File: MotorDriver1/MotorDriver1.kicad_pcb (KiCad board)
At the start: 2 copper layers, 60.5 x 66.5 mm, 74 parts, among them IC1 STM32C092RCT6, IC2 mcp6004-e_p, J1 GT-USB-7010ASV, J2 Conn_01x02, J3 Conn_01x02, Q1 IRLZ44N, Q2 IRLZ44N, Q3 IRLZ44N, Q4 IRLZ44N, SW1 K2-6639SP-C4SC-04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

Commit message: modifications to PCB layout
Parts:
- moved C_D1 20.5 mm to (166.2, 57.5)
- moved R17 20.5 mm to (166.3, 54.0)
- moved R18 20.5 mm to (169.8, 54.0)
- moved R19 20.5 mm to (169.8, 57.0)
- moved VR1 20.5 mm to (175.3, 54.0)
- moved VR2 20.5 mm to (183.3, 54.0)
- moved U3 9.51 mm to (175.5, 38.5), turned to 90 degrees
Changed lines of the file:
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@@
 	(footprint "Resistor_SMD:R_0402_1005Metric"
 		(layer "F.Cu")
-		(at 169 33.5)
+		(at 169.85 54)
 		(descr "Resistor SMD 0402 (1005 Metric), square (rectangular) end terminal, IPC-7351 nominal, (Body size source: IPC-SM-782 page 72, https://www.pcb-3d.com/wordpress/wp-content/uploads/ipc-sm-782a_amendment_1_and_2.pdf), generated with kicad-footprint-generator")
 		(tags "resistor")
@@
 	(footprint "Resistor_SMD:R_0402_1005Metric"
 		(layer "F.Cu")
-		(at 169 36.5)
+		(at 169.85 57)
 		(descr "Resistor SMD 0402 (1005 Metric), square (rectangular) end terminal, IPC-7351 nominal, (Body size source: IPC-SM-782 page 72, https://www.pcb-3d.com/wordpress/wp-content/uploads/ipc-sm-782a_amendment_1_and_2.pdf), generated with kicad-footprint-generator")
 		(tags "resistor")
@@
 	(footprint "Resistor_SMD:R_0402_1005Metric"
 		(layer "F.Cu")
-		(at 165.49 33.5)
+		(at 166.34 54)
 		(descr "Resistor SMD 0402 (1005 Metric), square (rectangular) end terminal, IPC-7351 nominal, (Body size source: IPC-SM-782 page 72, https://www.pcb-3d.com/wordpress/wp-content/uploads/ipc-sm-782a_amendment_1_and_2.pdf), generated with kicad-footprint-generator")
 		(tags "resistor")
@@
 	(footprint "footprintLib:XIAO-ESP32-C5-DIP"
 		(layer "F.Cu")
-		(at 175 48)
+		(at 175.5 38.5 90)
 		(property "Reference" "U3"
-			(at -0.275 -10.275 0)
+			(at -53.275 -5.775 90)
 			(unlocked yes)
 			(layer "F.SilkS")
@@
 		)
 		(property "Value" "XIAO-ESP32-C5-DIP"
-			(at 0 0 0)
+			(at 0 0 90)
 			(unlocked yes)
 			(layer "F.Fab")
@@
 		)
 		(property "Datasheet" ""
-			(at 0 0 0)
+			(at 0 0 90)
 			(unlocked yes)
 			(layer "F.Fab")
@@
 		)
 		(property "Description" ""
-			(at 0 0 0)
+			(at 0 0 90)
 			(unlocked yes)
 			(layer "F.Fab")
@@
 		(attr smd)
 		(fp_line
+			(start -8.509 -8.89)
+			(end 8.636 -8.89)
+			(stroke
+				(width 0.127)
+				(type solid)
+			)
+			(layer "F.SilkS")
+		)
+		(fp_line
 			(start -10.414 -6.985)
 			(end -10.414 6.985)
@@
 		)
 		(fp_line
-			(start -8.509 -8.89)
-			(end 8.636 -8.89)
+			(start 10.541 -4.495)
+			(end 11.551272 -4.491272)
 			(stroke
 				(width 0.127)
@@
 		)
 		(fp_line
-			(start -8.509 8.89)
-			(end 8.636 8.89)
+			(start 12.051 -3.991272)
+			(end 12.051 4.004)
 			(stroke
 				(width 0.127)
@@
 		)
 		(fp_line
-			(start 10.541 -4.495)
-			(end 11.551272 -4.491272)
+			(start 11.551 4.504)
+			(end 10.541 4.504)
 			(stroke
 				(width 0.127)
@@
 		)
 		(fp_line
-			(start 11.551 4.504)
-			(end 10.541 4.504)
+			(start -8.509 8.89)
+			(end 8.636 8.89)
 			(stroke
 				(width 0.127)
@@
 			(layer "F.SilkS")
 		)
-		(fp_line
-			(start 12.051 -3.991272)
-			(end 12.051 4.004)
+		(fp_arc
+			(start 8.636 -8.89)
+			(mid 9.983038 -8.332038)
+			(end 10.541 -6.985)
 			(stroke
 				(width 0.127)
@@
 		)
 		(fp_arc
-			(start -8.509 8.89)
-			(mid -9.856038 8.332038)
-			(end -10.414 6.985)
+			(start 11.551272 -4.491272)
+			(mid 11.904644 -4.344724)
+			(end 12.051 -3.991272)
 			(stroke
 				(width 0.127)
-				(type solid)
+				(type default)
 			)
 			(layer "F.SilkS")
 		)
 		(fp_arc
-			(start 8.636 -8.89)
-			(mid 9.983038 -8.332038)
-			(end 10.541 -6.985)
+			(start 12.051 4.004)
+			(mid 11.904553 4.357553)
+			(end 11.551 4.504)
 			(stroke
 				(width 0.127)
-				(type solid)
+				(type default)
 			)
 			(layer "F.SilkS")
@@
 		)
 		(fp_arc
-			(start 11.551272 -4.491272)
-			(mid 11.904644 -4.344724)
-			(end 12.051 -3.991272)
-			(stroke
-				(width 0.127)
-				(type default)
-			)
-			(layer "F.SilkS")
-		)
-		(fp_arc
-			(start 12.051 4.004)
-			(mid 11.904553 4.357553)
-			(end 11.551 4.504)
+			(start -8.509 8.89)
+			(mid -9.856038 8.332038)
+			(end -10.414 6.985)
 			(stroke
 				(width 0.127)
-				(type default)
+				(type solid)
 			)
 			(layer "F.SilkS")
 		)
 		(fp_circle
-			(center 9.37 -7.857)
-			(end 9.624 -7.857)
+			(center 10.25 -9)
+			(end 10.504 -9)
 			(stroke
 				(width 0.5)
@@
 		)
 		(fp_circle
-			(center 10.25 -9)
-			(end 10.504 -9)
+			(center 9.37 -7.857)
+			(end 9.624 -7.857)
 			(stroke
 				(width 0.5)
@@
 		)
 		(pad "1" smd roundrect
-			(at 7.62 -8.455 90)
+			(at 7.62 -8.455 180)
 			(size 2.432 1.524)
 			(layers "F.Cu" "F.Mask")
@@
 		)
 		(pad "1" thru_hole circle
-			(at 7.62 -7.62 90)
+			(at 7.62 -7.62 180)
 			(size 1.524 1.524)
 			(drill 0.889)
@@
 		)
 		(pad "2" smd roundrect
-			(at 5.08 -8.455 90)
+			(at 5.08 -8.455 180)
 			(size 2.432 1.524)
 			(layers "F.Cu" "F.Mask")
@@
 		)
 		(pad "2" thru_hole circle
-			(at 5.08 -7.62 90)
+			(at 5.08 -7.62 180)
 			(size 1.524 1.524)
 			(drill 0.889)
@@
 		)
 		(pad "3" smd roundrect
-			(at 2.54 -8.455 90)
+			(at 2.54 -8.455 180)
 			(size 2.432 1.524)
 			(layers "F.Cu" "F.Mask")
@@
 		)
 		(pad "3" thru_hole circle
-			(at 2.54 -7.62 90)
+			(at 2.54 -7.62 180)
 			(size 1.524 1.524)
 			(drill 0.889)
@@
 		)
 		(pad "4" smd roundrect
-			(at 0 -8.455 90)
+			(at 0 -8.455 180)
 			(size 2.432 1.524)
 			(layers "F.Cu" "F.Mask")
@@
 		)
 		(pad "4" thru_hole circle
-			(at 0 -7.62 90)
+			(at 0 -7.62 180)
 			(size 1.524 1.524)
 			(drill 0.889)
@@
 		)
 		(pad "5" smd roundrect
-			(at -2.54 -8.455 90)
+			(at -2.54 -8.455 180)
 			(size 2.432 1.524)
 			(layers "F.Cu" "F.Mask")
@@
 		)
 		(pad "5" thru_hole circle
-			(at -2.54 -7.62 90)
+			(at -2.54 -7.62 180)
 			(size 1.524 1.524)
 			(drill 0.889)
@@
 		)
 		(pad "6" smd roundrect
-			(at -5.08 -8.455 90)
+			(at -5.08 -8.455 180)
 			(size 2.432 1.524)
 			(layers "F.Cu" "F.Mask")
@@
 		)
 		(pad "6" thru_hole circle
-			(at -5.08 -7.62 90)
+			(at -5.08 -7.62 180)
 			(size 1.524 1.524)
 			(drill 0.889)
@@
 		)
 		(pad "7" smd roundrect
-			(at -7.62 -8.455 90)
+			(at -7.62 -8.455 180)
 			(size 2.432 1.524)
 			(layers "F.Cu" "F.Mask")
@@
 		)
 		(pad "7" thru_hole circle
-			(at -7.62 -7.62 90)
+			(at -7.62 -7.62 180)
 			(size 1.524 1.524)
 			(drill 0.889)
@@
 		)
 		(pad "8" thru_hole circle
-			(at -7.62 7.62 270)
+			(at -7.62 7.62)
 			(size 1.524 1.524)
 			(drill 0.889)
@@
 		)
 		(pad "8" smd roundrect
-			(at -7.62 8.455 270)
+			(at -7.62 8.455)
 			(size 2.432 1.524)
 			(layers "F.Cu" "F.Mask")
@@
 		)
 		(pad "9" thru_hole circle
-			(at -5.08 7.62 270)
+			(at -5.08 7.62)
 			(size 1.524 1.524)
 			(drill 0.889)
@@
 		)
 		(pad "9" smd roundrect
-			(at -5.08 8.455 270)
+			(at -5.08 8.455)
 			(size 2.432 1.524)
 			(layers "F.Cu" "F.Mask")
@@
 		)
 		(pad "10" thru_hole circle
-			(at -2.54 7.62 270)
+			(at -2.54 7.62)
 			(size 1.524 1.524)
 			(drill 0.889)
@@
 		)
 		(pad "10" smd roundrect
-			(at -2.54 8.455 270)
+			(at -2.54 8.455)
 			(size 2.432 1.524)
 			(layers "F.Cu" "F.Mask")
@@
 		)
 		(pad "11" thru_hole circle
-			(at 0 7.62 270)
+			(at 0 7.62)
 			(size 1.524 1.524)
 			(drill 0.889)
@@
 		)
 		(pad "11" smd roundrect
-			(at 0 8.455 270)
+			(at 0 8.455)
 			(size 2.432 1.524)
 			(layers "F.Cu" "F.Mask")
@@
 		)
 		(pad "12" thru_hole circle
-			(at 2.54 7.62 270)
+			(at 2.54 7.62)
 			(size 1.524 1.524)
 			(drill 0.889)
@@
 		)
 		(pad "12" smd roundrect
-			(at 2.54 8.455 270)
+			(at 2.54 8.455)
 			(size 2.432 1.524)
 			(layers "F.Cu" "F.Mask")
@@
 		)
 		(pad "13" thru_hole circle
-			(at 5.08 7.62 270)
+			(at 5.08 7.62)
 			(size 1.524 1.524)
 			(drill 0.889)
@@
 		)
 		(pad "13" smd roundrect
-			(at 5.08 8.455 270)
+			(at 5.08 8.455)
 			(size 2.432 1.524)
 			(layers "F.Cu" "F.Mask")
@@
 		)
 		(pad "14" thru_hole circle
-			(at 7.62 7.62 270)
+			(at 7.62 7.62)
 			(size 1.524 1.524)
 			(drill 0.889)
@@
 		)
 		(pad "14" smd roundrect
-			(at 7.62 8.455 270)
+			(at 7.62 8.455)
 			(size 2.432 1.524)
 			(layers "F.Cu" "F.Mask")
@@
 	(footprint "footprintLib:TS53YJ105MR10"
 		(layer "F.Cu")
-		(at 182.5 33.5)
+		(at 183.35 54)
 		(descr "TS53YJ105MR10-1")
 		(tags "Variable Resistor")
@@
 	(footprint "footprintLib:TS53YJ105MR10"
 		(layer "F.Cu")
-		(at 174.5 33.5)
+		(at 175.35 54)
 		(descr "TS53YJ105MR10-1")
 		(tags "Variable Resistor")
@@
 	(footprint "Capacitor_SMD:C_0201_0603Metric"
 		(layer "F.Cu")
-		(at 165.32 37)
+		(at 166.17 57.5)
 		(descr "Capacitor SMD 0201 (0603 Metric), square (rectangular) end terminal, IPC-7351 nominal, (Body size source: https://www.vishay.com/docs/20052/crcw0201e3.pdf), generated with kicad-footprint-generator")
 		(tags "capacitor")

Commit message: Re-layed out eo stuff
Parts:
- C12, C13, C14, R13, R14, U1: moved to B.Cu
- moved VR1 46.6 mm to (129.2, 60.8)
- moved VR2 46.6 mm to (137.2, 60.8)
- moved R17 29.8 mm to (137.1, 48.5)
- moved C_D1 29.8 mm to (136.9, 52.0)
- moved R18 29.8 mm to (140.6, 48.5)
- moved R19 29.8 mm to (140.6, 51.5)
- moved R15 15.3 mm to (160.0, 86.5), turned to 180 degrees
- moved R23 14.5 mm to (175.0, 51.8)
- moved R21 12.9 mm to (174.8, 53.8), turned to -90 degrees
- moved C13 11.7 mm to (168.5, 88.0)
- moved R22 11.6 mm to (173.7, 61.6), turned to 90 degrees
- moved R20 10.5 mm to (173.5, 63.6), turned to 180 degrees
- moved R12 9.70 mm to (159.5, 82.5), turned to -90 degrees
- moved C14 9.22 mm to (167.5, 90.0)
- moved U5 8.70 mm to (169.8, 53.8)
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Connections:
- IC1 pad 1: unconnected-(IC1-PC11-Pad1) -> USER_BTN
- IC1 pad 3: USER_BTN -> unconnected-(IC1-PC13-Pad3)
- U4 pad 4: FDCAN_STM -> FDCAN_RX_STM

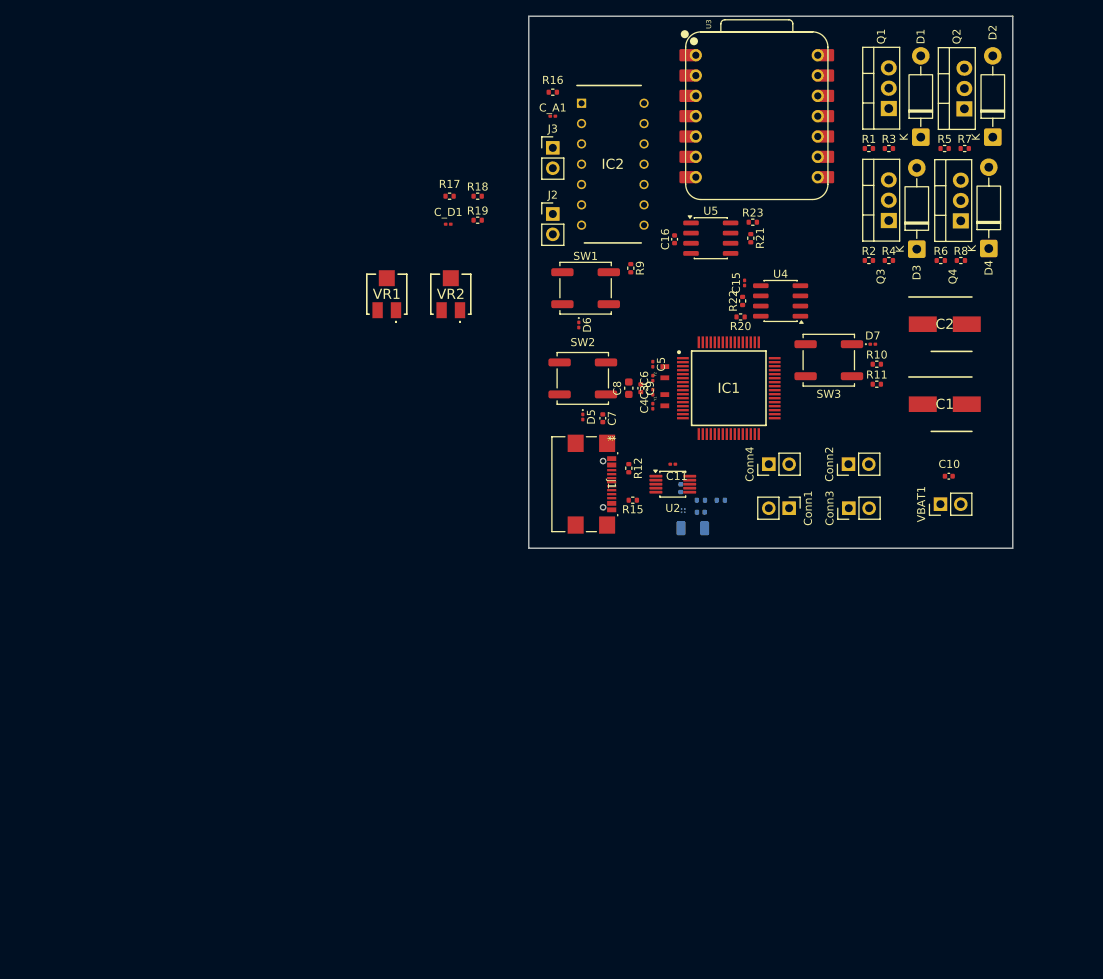
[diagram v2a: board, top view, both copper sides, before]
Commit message: component placing and first traces
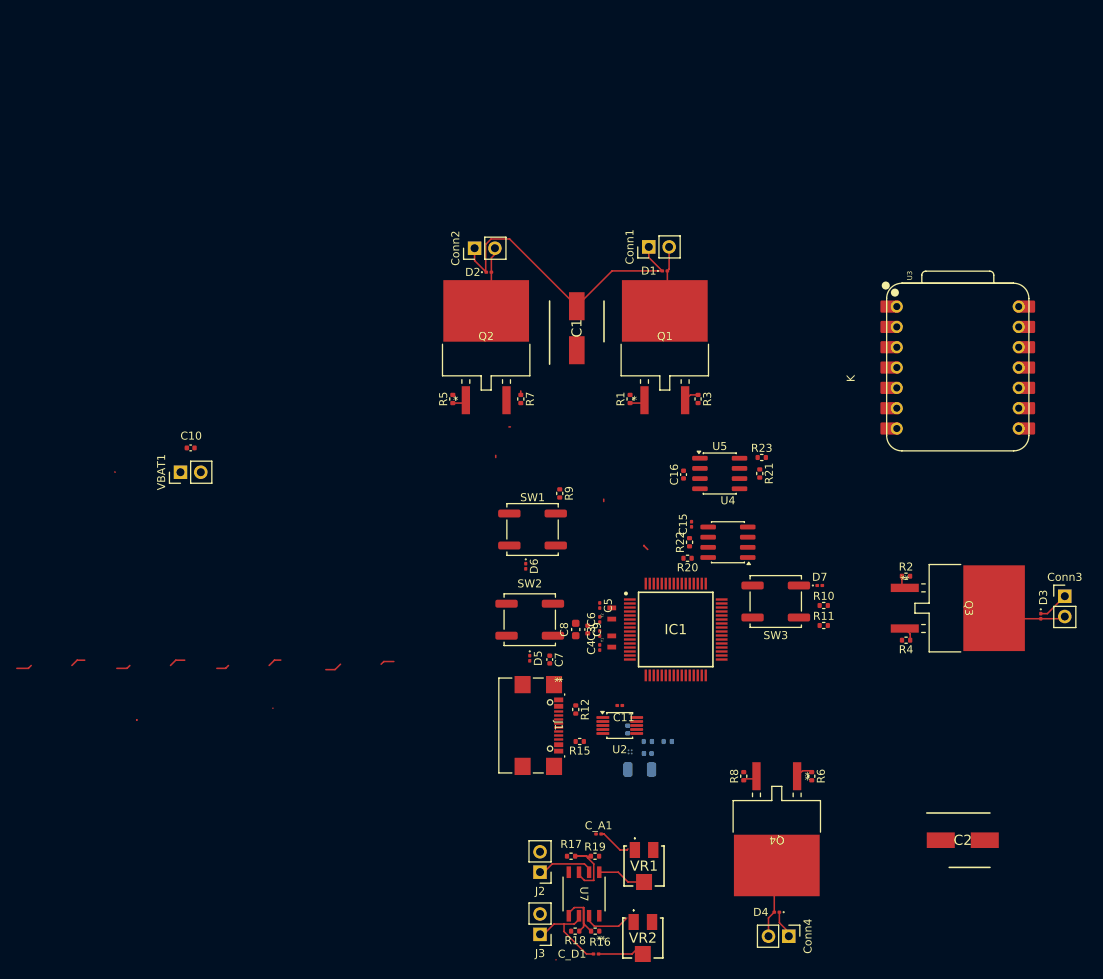
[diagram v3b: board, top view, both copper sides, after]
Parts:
- removed IC2: mcp6004-e_p, footprintLib:DIP781W56P254L1918H533Q14N
- added U7: LMV358AIDR, footprintLib:D8_TEX, F.Cu at (153.9, 135.7)
- D1, D2, D3, D4: value 1N4001 -> Power_D; footprint Diode_THT:D_DO-41_SOD81_P10.16mm_Horizontal -> Diode_SMD:D_0201_0603Metric
- Q1, Q2, Q3, Q4: value IRLZ44N -> IRLZ44NSTRLPBF; footprint Package_TO_SOT_THT:TO-220-3_Vertical -> footprintLib:NMOSGDS_D2PAK_INF
- moved R16 105.0 mm to (155.3, 140.4), turned to 180 degrees
- moved J3 98.3 mm to (148.4, 140.8), turned to 180 degrees
- moved VBAT1 95.1 mm to (103.5, 83.0)
- moved C10 94.8 mm to (104.7, 80.0)
- moved C_D1 93.1 mm to (155.4, 143.2)
- moved R18 92.7 mm to (152.8, 140.4), turned to 180 degrees
- moved C_A1 89.9 mm to (155.7, 128.2)
- moved D4 87.1 mm to (178.0, 138.0), turned to 180 degrees
- moved VR2 84.0 mm to (161.3, 141.2), turned to 180 degrees
- moved R17 83.9 mm to (152.3, 131.0)
- moved J2 82.3 mm to (148.4, 133.0), turned to 180 degrees
- moved R19 80.8 mm to (155.3, 131.0)
- moved Q4 80.8 mm to (178.0, 129.0), turned to 180 degrees
- moved VR1 78.4 mm to (161.4, 132.2), turned to 180 degrees
- moved R8 69.9 mm to (173.9, 121.0), turned to 90 degrees
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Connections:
- IC1 pad 47: Motor1_PWM -> Motor3_PWM
- IC1 pad 58: Motor3_PWM -> Motor1_PWM
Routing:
- net 5V: track 0.00 -> 46.1 mm
- net SensorDIn: track 0.00 -> 11.4 mm
- net /motorDriver/Motor4-: track 0.00 -> 10.3 mm
- net /motorDriver/Motor3-: track 0.00 -> 9.77 mm
- net SensorA_0.5V: track 0.00 -> 9.71 mm
- net /motorDriver/Motor1-: track 0.00 -> 9.15 mm
- net SensorD_0.5V: track 0.00 -> 8.99 mm
- net /motorDriver/Motor2-: track 0.00 -> 8.29 mm
- net SensorAIn: track 0.00 -> 6.75 mm
- net SensorDOut: track 0.00 -> 6.06 mm
- net SensorAOut: track 0.00 -> 5.10 mm
- net Net-(VR2-WIPER): track 0.00 -> 4.89 mm
- net Net-(VR1-CCW): track 0.00 -> 4.23 mm
- net Motor4_PWM: track 0.00 -> 4.22 mm
- net Motor1_PWM: track 0.00 -> 3.90 mm
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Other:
- board outline removed

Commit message: Updated crystal footprints
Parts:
- C3, C4: value 6 pF -> 8 pF
- C5, C6: value 5 pF -> 7.5 pF, 0.1%
- Y1: footprint footprintLib:XTAL_ECS-.327-12.5-12R-TR -> footprintLib:ECS-480-8-30-JGN-TR
- Y2: footprint footprintLib:XTAL_ECS-.327-12.5-12R-TR -> footprintLib:MU00527-32.768K
- moved C7 5.12 mm to (144.5, 106.2)
- moved D5 5.12 mm to (142.0, 106.1)
- moved SW2 5.12 mm to (142.0, 101.2)
- moved C8 3.12 mm to (149.8, 102.7)
- moved C9 3.12 mm to (151.2, 102.7)
- moved C4 2.41 mm to (153.8, 106.1)
- moved C3 2.35 mm to (153.8, 104.2)
- moved C5 1.01 mm to (155.0, 99.2)
- moved C6 1.01 mm to (155.0, 100.9)
- moved Y2 1.01 mm to (156.5, 100.2)
- moved Y1 0.87 mm to (156.5, 104.2)
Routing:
- net Motor4_PWM: track 4.22 -> 2.11 mm
- net Net-(Q2-S): track 2.56 -> 0.50 mm
- net Motor1_PWM: track 3.90 -> 1.95 mm
- net Net-(Q1-S): track 3.78 -> 1.89 mm
- net Motor2_PWM: track 3.56 -> 1.78 mm
- net Net-(Q3-S): track 3.48 -> 1.74 mm
- net Net-(Q4-S): track 3.46 -> 1.73 mm
- net Motor3_PWM: track 3.22 -> 1.61 mm
- net /motorDriver/Motor4-: track 10.3 -> 9.27 mm

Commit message: Exported final JLCPCB files
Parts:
- removed R13, R14: 10k, 1%, Resistor_SMD:R_0402_1005Metric
- added C17: 100 nF, Capacitor_SMD:C_0402_1005Metric, F.Cu at (153.0, 112.5)
- added C18: 100 nF, Capacitor_SMD:C_0402_1005Metric, F.Cu at (144.0, 79.5)
- added C19: 100 nF, Capacitor_SMD:C_0402_1005Metric, F.Cu at (157.5, 79.8)
- added G***: LOGO, LOGO, F.Cu at (185.0, 122.5)
- C10, C16: value 100nF -> 100 nF
- C11, C5, C6: footprint Capacitor_SMD:C_0201_0603Metric -> Capacitor_SMD:C_0402_1005Metric
- C12: value 100nF -> 100 nF; moved to F.Cu
- C13: value 100nF -> 1 uF; footprint Capacitor_SMD:C_0402_1005Metric -> Capacitor_SMD:C_0603_1608Metric; moved to F.Cu
- C14: value 10uF -> 1 uF; footprint Capacitor_SMD:C_1206_3216Metric -> Capacitor_SMD:C_0603_1608Metric; moved to F.Cu
- C15: value 100nF -> 100 nF; footprint Capacitor_SMD:C_0201_0603Metric -> Capacitor_SMD:C_0402_1005Metric
- C3, C4: value 8 pF -> 8 pF, 0.1%; footprint Capacitor_SMD:C_0201_0603Metric -> Capacitor_SMD:C_0402_1005Metric
- C_A1, C_D1: value 44nF -> 47 nF; footprint Capacitor_SMD:C_0201_0603Metric -> Capacitor_SMD:C_0402_1005Metric
- D1, D2, D3, D4: value Power_D -> SM5819L2-TP; footprint Diode_SMD:D_0201_0603Metric -> footprintLib:SDO_SM5819L2-TP_MCE
- D5, D6, D7: value ESDALC6V1-1U2 -> ESDALC6V1-1M2; footprint Diode_SMD:D_0201_0603Metric -> Diode_SMD:D_0402_1005Metric
- R1, R16, R17, R2, R5, R6: value 10000 -> 10k
- R18, R19: value 1800 -> 1.8k
- R3, R4, R7, R8: footprint Resistor_SMD:R_0402_1005Metric -> Resistor_SMD:R_1206_3216Metric
- U1: value TPS22916CNYFPR -> NCP361SNT1G; footprint footprintLib:TPS22916CNYFPR -> footprintLib:SOT95P275X110-5N; moved to F.Cu
- moved VBAT1 73.7 mm to (177.0, 78.0)
- moved C10 45.8 mm to (141.9, 106.7), turned to 90 degrees
- moved C2 34.3 mm to (180.8, 101.5)
- moved D1 34.0 mm to (130.0, 57.0)
- moved Conn1 34.0 mm to (128.0, 54.0)
- moved Q1 34.0 mm to (130.0, 65.1)
- moved R1 34.0 mm to (125.7, 73.0)
- moved R3 33.2 mm to (135.0, 73.0)
- moved VR2 33.1 mm to (158.5, 108.3), turned to 90 degrees
- moved Conn3 32.0 mm to (184.0, 87.2)
- moved D3 31.8 mm to (181.5, 89.2)
- moved Q3 31.4 mm to (172.9, 88.2)
- moved R2 31.4 mm to (165.0, 84.2)
- moved R4 30.8 mm to (165.0, 94.0)
- moved C12 28.8 mm to (130.6, 113.6)
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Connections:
- net /FDCAN/CANH renamed /FDCAN/CAN_P
- net /FDCAN/CANL renamed /FDCAN/CAN_N
- C1 pad 1: GND -> 5V
- C1 pad 2: 5V -> GND
- C13 pad 2: 5V_USB -> VBUS
- C2 pad 1: GND -> 5V
- C2 pad 2: 5V -> GND
- C_A1 pad 1: SensorAIn -> SensorAOut
- C_A1 pad 2: Net-(VR1-CCW) -> SensorAIn
- C_D1 pad 2: Net-(VR2-WIPER) -> SensorDOut
- SW1 pad 1: Net-(R9-Pad2) -> unconnected-(SW1-Pad1)
- SW1 pad 3: USER_BTN -> unconnected-(SW1-Pad3)
- SW2 pad 1: GND -> unconnected-(SW2-Pad1)
- SW2 pad 3: NRST -> unconnected-(SW2-Pad3)
- SW3 pad 1: 3V3 -> unconnected-(SW3-Pad1)
- SW3 pad 3: BOOT -> unconnected-(SW3-Pad3)
- VR1 pad A1: Net-(VR1-CCW) -> SensorAIn
- VR2 pad A1: SensorDOut -> SensorDIn
- VR2 pad B1: Net-(VR2-WIPER) -> SensorDOut
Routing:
- net 5V: track 45.8 -> 109.6 mm, vias 0 -> 4
- net 3V3: track 0.00 -> 31.8 mm, vias 0 -> 9
- net Motor1_PWM: track 1.95 -> 32.5 mm
- net FDCAN_RX_ESP: track 0.00 -> 28.8 mm
- net FDCAN_STBY_ESP: track 0.00 -> 27.0 mm, vias 0 -> 1
- net NRST: track 0.00 -> 24.9 mm
- net !DTR: track 0.00 -> 22.6 mm, vias 0 -> 2
- net Motor4_PWM: track 2.11 -> 24.2 mm, vias 0 -> 2
- net FDCAN_TX_STM: track 0.00 -> 21.9 mm
- net /FDCAN/CAN_P: track 0.00 -> 19.3 mm
- net USER_BTN: track 0.00 -> 19.1 mm
- net /FDCAN/CAN_N: track 0.00 -> 18.8 mm
- net Motor2_PWM: track 1.78 -> 20.4 mm, vias 0 -> 2
- net !RTS: track 0.00 -> 17.8 mm, vias 0 -> 2
- net BOOT: track 0.00 -> 16.9 mm
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- added copper zone on In2.Cu, net 3V3
- added copper zone on In2.Cu, net 5V
- added copper zone on B.Cu, net GND
- added copper zone on F.Cu, net GND
- added copper zone on In1.Cu, net GND
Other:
- board outline added: 72 x 76 mm
- copper layers 2 -> 4
- board text added: "+"
- board text added: "-"
- board text added: "3V3"
- board text added: "5V"
- board text added: "72 x 76 mm"
- board text added: "BOOT"
- board text added: "Battery"
- board text added: "Emma Ouyang, Emma Steinberg, Ashley Luo, Siyang Sun"
- board text added: "FDCAN STBY"
- board text added: "GND"
- board text added: "Motor1"
- board text added: "Motor2"
- board text added: "Motor3"
- board text added: "Motor4"
- board text added: "NRST"
- board text added: "RX"
- board text added: "STM32C092RCT6"
- board text added: "SaddleReady"
- board text added: "Sensor Inputs"
- board text added: "TX"
- board text added: "USER"
